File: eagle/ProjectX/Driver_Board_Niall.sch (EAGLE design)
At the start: 182 parts, among them IC2 NCV78M05BDTRKG, J1 694102303002, U1 TC4427AEOA, U10 TC4427AEOA, U11 TC4427AEOA, U12 TC4427AEOA, U1200 CD74HC4067SM96, U13 TC4427AEOA, U14 TC4427AEOA, U15 TC4427AEOA, U16 TC4427AEOA, U17 TC4427AEOA, U18 TC4427AEOA, U19 TC4427AEOA, U2 TC4427AEOA, U20 TC4427AEOA, U200 ADA4091-2ARZ-RL, U21 TC4427AEOA, U22 TC4427AEOA, U23 TC4427AEOA, U24 TC4427AEOA, U25 TC4427AEOA, U26 TC4427AEOA, U27 TC4427AEOA, U28 TC4427AEOA, U29 TC4427AEOA, U3 TC4427AEOA, U30 TC4427AEOA, U31 TC4427AEOA, U32 TC4427AEOA, U33 TC4427AEOA, U34 TC4427AEOA, U35 TC4427AEOA, U36 TC4427AEOA, U37 TC4427AEOA, U38 TC4427AEOA, U39 TC4427AEOA, U4 TC4427AEOA, U40 TC4427AEOA, U41 TC4427AEOA, U42 TC4427AEOA, U43 TC4427AEOA, U44 TC4427AEOA, U45 TC4427AEOA, U46 TC4427AEOA, U47 TC4427AEOA, U48 TC4427AEOA, U49 TC4427AEOA, U5 TC4427AEOA, U50 TC4427AEOA, U6 TC4427AEOA, U7 TC4427AEOA, U8 TC4427AEOA, U9 TC4427AEOA

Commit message: Added capasitors to inputs
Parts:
- added C51, C52, C53: 100nF, resistor:C-EUC0805
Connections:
- net +5V: now also C51.1, C52.1, C53.1; no longer DIP2.5V@1
- net GND: now also C51.2, C52.2, C53.2; no longer DIP2.GND@1, DIP2.GND@2, DIP2.GND@3
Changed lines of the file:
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@@
 <part name="U1200" library="SnapEDA-Library (3)" deviceset="CD74HC4067SM96" device=""/>
 <part name="SUPPLY2" library="supply1" library_urn="urn:adsk.eagle:library:371" deviceset="GND" device=""/>
-<part name="GND3" library="supply1" library_urn="urn:adsk.eagle:library:371" deviceset="GND" device=""/>
 <part name="GND4" library="supply1" library_urn="urn:adsk.eagle:library:371" deviceset="GND" device=""/>
-<part name="GND5" library="supply1" library_urn="urn:adsk.eagle:library:371" deviceset="GND" device=""/>
-<part name="GND6" library="supply1" library_urn="urn:adsk.eagle:library:371" deviceset="GND" device=""/>
 <part name="SUPPLY3" library="supply2" library_urn="urn:adsk.eagle:library:372" deviceset="+5V" device=""/>
-<part name="SUPPLY4" library="supply2" library_urn="urn:adsk.eagle:library:372" deviceset="+5V" device=""/>
 <part name="DIP2" library="Parts" deviceset="CORE3S500E" device="SMT"/>
 <part name="5V-REG" library="Parts" deviceset="OKI-78SR" device=""/>
@@
 <part name="SUPPLY167" library="supply1" library_urn="urn:adsk.eagle:library:371" deviceset="GND" device=""/>
 <part name="SUPPLY168" library="supply1" library_urn="urn:adsk.eagle:library:371" deviceset="GND" device=""/>
+<part name="C51" library="resistor" library_urn="urn:adsk.eagle:library:348" deviceset="C-EU" device="C0805" package3d_urn="urn:adsk.eagle:package:26137/1" value="100nF"/>
+<part name="GND3" library="supply1" library_urn="urn:adsk.eagle:library:371" deviceset="GND" device=""/>
+<part name="C52" library="resistor" library_urn="urn:adsk.eagle:library:348" deviceset="C-EU" device="C0805" package3d_urn="urn:adsk.eagle:package:26137/1" value="100nF"/>
+<part name="GND5" library="supply1" library_urn="urn:adsk.eagle:library:371" deviceset="GND" device=""/>
+<part name="C53" library="resistor" library_urn="urn:adsk.eagle:library:348" deviceset="C-EU" device="C0805" package3d_urn="urn:adsk.eagle:package:26137/1" value="100nF"/>
+<part name="GND6" library="supply1" library_urn="urn:adsk.eagle:library:371" deviceset="GND" device=""/>
 </parts>
 <sheets>
@@
 <attribute name="VALUE" x="-25.4" y="-43.18" size="1.778" layer="96" rot="MR0"/>
 </instance>
-<instance part="GND3" gate="1" x="-96.52" y="421.64" rot="R270">
-<attribute name="VALUE" x="-99.06" y="424.18" size="1.778" layer="96" rot="R270"/>
-</instance>
 <instance part="GND4" gate="1" x="-96.52" y="393.7" rot="R270">
 <attribute name="VALUE" x="-99.06" y="396.24" size="1.778" layer="96" rot="R270"/>
 </instance>
-<instance part="GND5" gate="1" x="2.54" y="393.7" rot="R90">
-<attribute name="VALUE" x="5.08" y="391.16" size="1.778" layer="96" rot="R90"/>
-</instance>
-<instance part="GND6" gate="1" x="2.54" y="421.64" rot="R90">
-<attribute name="VALUE" x="5.08" y="419.1" size="1.778" layer="96" rot="R90"/>
-</instance>
 <instance part="SUPPLY3" gate="+5V" x="-60.96" y="393.7" rot="R270">
 <attribute name="VALUE" x="-57.785" y="395.605" size="1.778" layer="96" rot="R270"/>
 </instance>
-<instance part="SUPPLY4" gate="+5V" x="-33.02" y="393.7" rot="R90">
-<attribute name="VALUE" x="-36.195" y="391.795" size="1.778" layer="96" rot="R90"/>
-</instance>
 <instance part="DIP2" gate="G$1" x="-45.72" y="421.64"/>
 <instance part="5V-REG" gate="G$1" x="96.52" y="167.64">
@@
 <attribute name="VALUE" x="-386.842" y="43.942" size="1.778" layer="96" rot="MR270"/>
 </instance>
+<instance part="C51" gate="G$1" x="-60.96" y="355.6" rot="R90">
+<attribute name="NAME" x="-61.341" y="357.124" size="1.778" layer="95" rot="R90"/>
+<attribute name="VALUE" x="-56.261" y="357.124" size="1.778" layer="96" rot="R90"/>
+</instance>
+<instance part="GND3" gate="1" x="-53.34" y="355.6" rot="R90">
+<attribute name="VALUE" x="-50.8" y="353.06" size="1.778" layer="96" rot="R90"/>
+</instance>
+<instance part="C52" gate="G$1" x="20.32" y="134.62" rot="R180">
+<attribute name="NAME" x="18.796" y="134.239" size="1.778" layer="95" rot="R180"/>
+<attribute name="VALUE" x="18.796" y="139.319" size="1.778" layer="96" rot="R180"/>
+</instance>
+<instance part="GND5" gate="1" x="20.32" y="142.24" rot="R180">
+<attribute name="VALUE" x="22.86" y="144.78" size="1.778" layer="96" rot="R180"/>
+</instance>
+<instance part="C53" gate="G$1" x="-27.94" y="39.116" rot="R180">
+<attribute name="NAME" x="-29.464" y="38.735" size="1.778" layer="95" rot="R180"/>
+<attribute name="VALUE" x="-29.464" y="43.815" size="1.778" layer="96" rot="R180"/>
+</instance>
+<instance part="GND6" gate="1" x="-27.94" y="46.736" rot="R180">
+<attribute name="VALUE" x="-25.4" y="49.276" size="1.778" layer="96" rot="R180"/>
+</instance>
 </instances>
 <busses>
@@
 </segment>
 <segment>
-<pinref part="GND3" gate="1" pin="GND"/>
-<wire x1="-88.9" y1="421.64" x2="-93.98" y2="421.64" width="0.1524" layer="91"/>
-<pinref part="DIP2" gate="G$1" pin="GND@2"/>
-</segment>
-<segment>
-<pinref part="GND6" gate="1" pin="GND"/>
-<wire x1="-5.08" y1="421.64" x2="0" y2="421.64" width="0.1524" layer="91"/>
-<pinref part="DIP2" gate="G$1" pin="GND@1"/>
-</segment>
-<segment>
-<pinref part="GND5" gate="1" pin="GND"/>
-<wire x1="-5.08" y1="393.7" x2="0" y2="393.7" width="0.1524" layer="91"/>
-<pinref part="DIP2" gate="G$1" pin="GND@3"/>
-</segment>
-<segment>
 <pinref part="5V-REG" gate="G$1" pin="GND"/>
 <pinref part="GND7" gate="1" pin="GND"/>
@@
 <pinref part="2" gate="G$1" pin="22"/>
 </segment>
+<segment>
+<pinref part="C51" gate="G$1" pin="2"/>
+<pinref part="GND3" gate="1" pin="GND"/>
+</segment>
+<segment>
+<pinref part="C52" gate="G$1" pin="2"/>
+<pinref part="GND5" gate="1" pin="GND"/>
+</segment>
+<segment>
+<pinref part="C53" gate="G$1" pin="2"/>
+<pinref part="GND6" gate="1" pin="GND"/>
+</segment>
 </net>
 <net name="N$5" class="0">
@@
 <wire x1="-66.04" y1="393.7" x2="-63.5" y2="393.7" width="0.1524" layer="91"/>
 <pinref part="DIP2" gate="G$1" pin="5V@2"/>
-</segment>
-<segment>
-<pinref part="DIP2" gate="G$1" pin="5V@1"/>
-<pinref part="SUPPLY4" gate="+5V" pin="+5V"/>
-<wire x1="-30.48" y1="393.7" x2="-27.94" y2="393.7" width="0.1524" layer="91"/>
+<wire x1="-63.5" y1="393.7" x2="-63.5" y2="355.6" width="0.1524" layer="91"/>
+<junction x="-63.5" y="393.7"/>
+<pinref part="C51" gate="G$1" pin="1"/>
+<wire x1="-63.5" y1="355.6" x2="-63.5" y2="350.52" width="0.1524" layer="91"/>
+<junction x="-63.5" y="355.6"/>
 </segment>
 <segment>
@@
 <pinref part="U1200" gate="A" pin="VCC"/>
 <pinref part="SUPPLY82" gate="+5V" pin="+5V"/>
+<pinref part="C53" gate="G$1" pin="1"/>
+<wire x1="-27.94" y1="33.02" x2="-27.94" y2="36.576" width="0.1524" layer="91"/>
+<junction x="-27.94" y="33.02"/>
 </segment>
 <segment>
@@
 <wire x1="15.24" y1="132.08" x2="20.32" y2="132.08" width="0.1524" layer="91"/>
 <pinref part="U$1" gate="G$1" pin="VIN"/>
+<pinref part="C52" gate="G$1" pin="1"/>
+<junction x="20.32" y="132.08"/>
 </segment>
 <segment>

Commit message: Niall board more work
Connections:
- net 3: now also DIP2.8; no longer DIP2.35
- net GND: now also DIP2.GND@2; no longer DIP2.GND@4
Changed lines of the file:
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@@
 <part name="U1200" library="SnapEDA-Library (3)" deviceset="CD74HC4067SM96" device=""/>
 <part name="SUPPLY2" library="supply1" library_urn="urn:adsk.eagle:library:371" deviceset="GND" device=""/>
-<part name="GND4" library="supply1" library_urn="urn:adsk.eagle:library:371" deviceset="GND" device=""/>
 <part name="SUPPLY3" library="supply2" library_urn="urn:adsk.eagle:library:372" deviceset="+5V" device=""/>
 <part name="DIP2" library="Parts" deviceset="CORE3S500E" device="SMT"/>
@@
 <part name="C53" library="resistor" library_urn="urn:adsk.eagle:library:348" deviceset="C-EU" device="C0805" package3d_urn="urn:adsk.eagle:package:26137/1" value="100nF"/>
 <part name="GND6" library="supply1" library_urn="urn:adsk.eagle:library:371" deviceset="GND" device=""/>
+<part name="GND8" library="supply1" library_urn="urn:adsk.eagle:library:371" deviceset="GND" device=""/>
 </parts>
 <sheets>
@@
 <attribute name="VALUE" x="-25.4" y="-43.18" size="1.778" layer="96" rot="MR0"/>
 </instance>
-<instance part="GND4" gate="1" x="-96.52" y="393.7" rot="R270">
-<attribute name="VALUE" x="-99.06" y="396.24" size="1.778" layer="96" rot="R270"/>
-</instance>
 <instance part="SUPPLY3" gate="+5V" x="-60.96" y="393.7" rot="R270">
 <attribute name="VALUE" x="-57.785" y="395.605" size="1.778" layer="96" rot="R270"/>
@@
 <attribute name="VALUE" x="-25.4" y="49.276" size="1.778" layer="96" rot="R180"/>
 </instance>
+<instance part="GND8" gate="1" x="-91.44" y="421.64" rot="R270">
+<attribute name="VALUE" x="-93.98" y="424.18" size="1.778" layer="96" rot="R270"/>
+</instance>
 </instances>
 <busses>
@@
 <net name="GND" class="0">
 <segment>
-<pinref part="GND4" gate="1" pin="GND"/>
-<wire x1="-88.9" y1="393.7" x2="-93.98" y2="393.7" width="0.1524" layer="91"/>
-<pinref part="DIP2" gate="G$1" pin="GND@4"/>
-</segment>
-<segment>
 <pinref part="5V-REG" gate="G$1" pin="GND"/>
 <pinref part="GND7" gate="1" pin="GND"/>
@@
 <pinref part="GND6" gate="1" pin="GND"/>
 </segment>
+<segment>
+<pinref part="DIP2" gate="G$1" pin="GND@2"/>
+<pinref part="GND8" gate="1" pin="GND"/>
+</segment>
 </net>
 <net name="N$5" class="0">
@@
 </segment>
 <segment>
-<pinref part="DIP2" gate="G$1" pin="35"/>
-<wire x1="-88.9" y1="396.24" x2="-106.68" y2="396.24" width="0.1524" layer="91"/>
-<label x="-104.14" y="396.24" size="1.778" layer="95"/>
+<pinref part="DIP2" gate="G$1" pin="8"/>
+<wire x1="-88.9" y1="419.1" x2="-106.68" y2="419.1" width="0.1524" layer="91"/>
+<label x="-101.6" y="419.1" size="1.778" layer="95"/>
 </segment>
 </net>

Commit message: More cleaning
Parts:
- added C54: 100nF, resistor:C-EUC0805
- added UA78M05CDCY: (no value), linear-technology:LT1129CST5
- C53: value 100nF -> 330nF
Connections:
- new net N$23: C54.2, U1200.VCC, UA78M05CDCYG$1.OUT
- net +5V: no longer C53.1, U1200.VCC
- net GND: now also C53.1, C54.1, DIP2.GND@4, UA78M05CDCYG$1.GND; no longer C53.2, DIP2.GND@2
- net VDD: now also C53.2, UA78M05CDCYG$1.IN
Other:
- moved on the sheet: C53

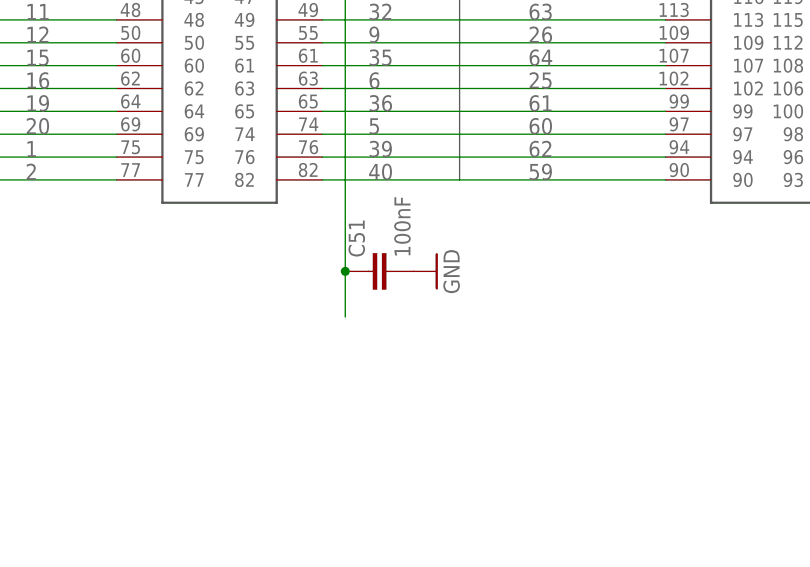
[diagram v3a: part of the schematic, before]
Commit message: More DRC fixes, just about all done
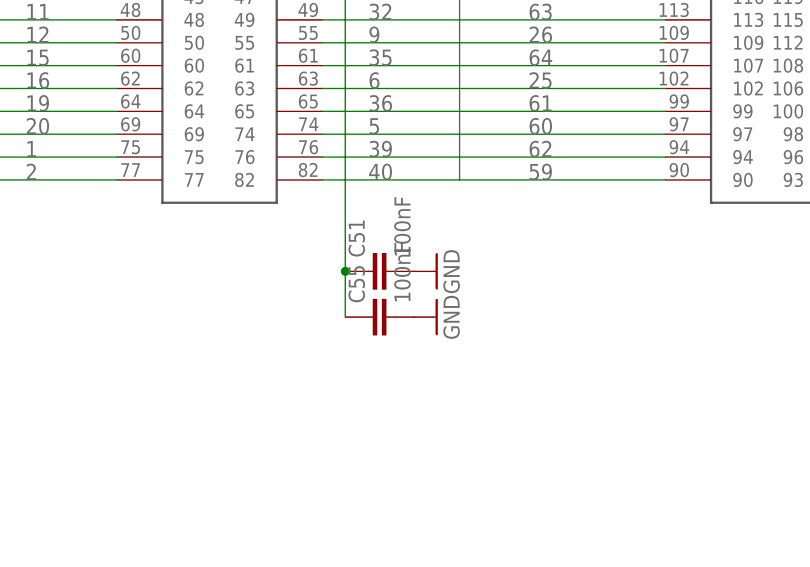
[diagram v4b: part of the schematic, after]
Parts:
- added C55: 100nF, resistor:C-EUC0805
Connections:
- net +5V: now also C55.1
- net GND: now also C55.2
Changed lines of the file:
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@@
 <part name="UA78M05CDCY" library="linear-technology" library_urn="urn:adsk.eagle:library:261" deviceset="LT1129CST5" device="" package3d_urn="urn:adsk.eagle:package:16063/1"/>
 <part name="C54" library="resistor" library_urn="urn:adsk.eagle:library:348" deviceset="C-EU" device="C0805" package3d_urn="urn:adsk.eagle:package:26137/1" value="100nF"/>
+<part name="C55" library="resistor" library_urn="urn:adsk.eagle:library:348" deviceset="C-EU" device="C0805" package3d_urn="urn:adsk.eagle:package:26137/1" value="100nF"/>
+<part name="GND4" library="supply1" library_urn="urn:adsk.eagle:library:371" deviceset="GND" device=""/>
 </parts>
 <sheets>
@@
 <attribute name="NAME" x="24.384" y="45.085" size="1.778" layer="95"/>
 <attribute name="VALUE" x="24.384" y="40.005" size="1.778" layer="96"/>
+</instance>
+<instance part="C55" gate="G$1" x="-60.96" y="350.52" rot="R90">
+<attribute name="NAME" x="-61.341" y="352.044" size="1.778" layer="95" rot="R90"/>
+<attribute name="VALUE" x="-56.261" y="352.044" size="1.778" layer="96" rot="R90"/>
+</instance>
+<instance part="GND4" gate="1" x="-53.34" y="350.52" rot="R90">
+<attribute name="VALUE" x="-50.8" y="347.98" size="1.778" layer="96" rot="R90"/>
 </instance>
 </instances>
@@
 <wire x1="-93.98" y1="393.7" x2="-88.9" y2="393.7" width="0.1524" layer="91"/>
 </segment>
+<segment>
+<pinref part="C55" gate="G$1" pin="2"/>
+<pinref part="GND4" gate="1" pin="GND"/>
+</segment>
 </net>
 <net name="N$5" class="0">
@@
 <wire x1="-63.5" y1="355.6" x2="-63.5" y2="350.52" width="0.1524" layer="91"/>
 <junction x="-63.5" y="355.6"/>
-</segment>
-<segment>
+<pinref part="C55" gate="G$1" pin="1"/>
+</segment>
+<segment>

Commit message: Bit more work
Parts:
- added C56: 100nF, resistor:C-EUC0805
- added J2: 694102303002, SnapEDA-Library:694102303002
- added JP1: JUMPER-SMT_2_NC_TRACE_SILK, SparkFun-Jumpers:JUMPER-SMT_2_NC_TRACE_SILK
- added JP3: JUMPER-SMT_2_NO_SILK, SparkFun-Jumpers:JUMPER-SMT_2_NO_SILK
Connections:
- new net N$24: 5V-REG.IN, J2.1, JP1.1
- new net N$25: C52.1, C56.1, JP3.1, U$1.VIN
- net +5V: now also JP3.2; no longer C52.1, U$1.VIN
- net GND: now also C56.2, J2.2
- net VDD: now also JP1.2; no longer 5V-REG.IN
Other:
- moved on the sheet: 5V-REG, C52, J1

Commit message: Niall driver board finished draft 1
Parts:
- removed LED_1, LED_10, LED_2, LED_3, LED_4, LED_5, LED_6, LED_7, LED_8, LED_9: 1655, SnapEDA-Library (5):1655
- added DATA_3: (no value), con-lstb:MA05-2
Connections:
- removed net N$13: LED_2.DOUT, LED_3.DIN
- removed net N$15: LED_3.DOUT, LED_4.DIN
- removed net N$16: LED_4.DOUT, LED_5.DIN
- removed net N$17: LED_5.DOUT, LED_6.DIN
- removed net N$18: LED_6.DOUT, LED_7.DIN
- removed net N$19: LED_7.DOUT, LED_8.DIN
- removed net N$20: LED_8.DOUT, LED_9.DIN
- removed net N$21: LED_10.DIN, LED_9.DOUT
- removed net N$22: LED_1.DIN, U$1.6
- removed net N$9: LED_1.DOUT, LED_2.DIN
- new net FPGA_1: DATA_1.1, DIP2.35
- new net FPGA_10: DATA_2.7, DIP2.197
- new net FPGA_11: DATA_2.5, DIP2.200
- new net FPGA_12: DATA_2.3, DIP2.203
- new net FPGA_13: DATA_2.1, DIP2.2
- new net FPGA_2: DATA_1.3, DIP2.33
- new net FPGA_3: DATA_1.5, DIP2.30
- new net FPGA_4: DATA_1.7, DIP2.28
- new net TEENSY_DATA_24: DATA_3.2, U$1.24
- new net TEENSY_DATA_25: DATA_3.1, U$1.25
- new net TEENSY_DATA_26: DATA_3.3, U$1.26
- new net TEENSY_DATA_27: DATA_3.4, U$1.27
- new net TEENSY_DATA_29: DATA_3.6, U$1.29
- new net TEENSY_DATA_30: DATA_3.5, U$1.30
- new net TEENSY_DATA_6: DIP2.15, U$1.6
- net +5V: now also DATA_1.10, DATA_2.10, DATA_3.10; no longer LED_1.VDD, LED_10.VDD, LED_2.VDD, LED_3.VDD, LED_4.VDD, LED_5.VDD, LED_6.VDD, LED_7.VDD, LED_8.VDD, LED_9.VDD
- net GND: now also DATA_1.9, DATA_2.9, DATA_3.9; no longer LED_1.VSS, LED_10.VSS, LED_2.VSS, LED_3.VSS, LED_4.VSS, LED_5.VSS, LED_6.VSS, LED_7.VSS, LED_8.VSS, LED_9.VSS
- net TEENSY_DATA_0: now also DATA_1.2
- net TEENSY_DATA_1: now also DATA_1.4
- net TEENSY_DATA_10: now also DATA_2.4
- net TEENSY_DATA_11: now also DATA_2.6
- net TEENSY_DATA_12: now also DATA_2.8
- net TEENSY_DATA_2: now also DATA_1.6
- net TEENSY_DATA_3: now also DATA_1.8
- net TEENSY_DATA_31: now also DATA_3.7
- net TEENSY_DATA_32: now also DATA_3.8
- net TEENSY_DATA_4: now also DIP2.24
- net TEENSY_DATA_5: now also DIP2.11
- net TEENSY_DATA_7: now also DIP2.18
- net TEENSY_DATA_8: now also DIP2.22
- net TEENSY_DATA_9: now also DATA_2.2
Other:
- moved on the sheet: DATA_1, DATA_2
